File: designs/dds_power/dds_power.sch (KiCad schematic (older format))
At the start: 25 parts, among them K1 3.3_1.8, K2 3.3_1.8, K3 3.3_1.8, K4 3.3_1.8, K5 3.3_1.8, K6 3.3_1.8, P1 CONN_3, P2 12V, P3 12V, P4 12V, P5 12V, P6 12V, P7 12V, U1 QD48T018033

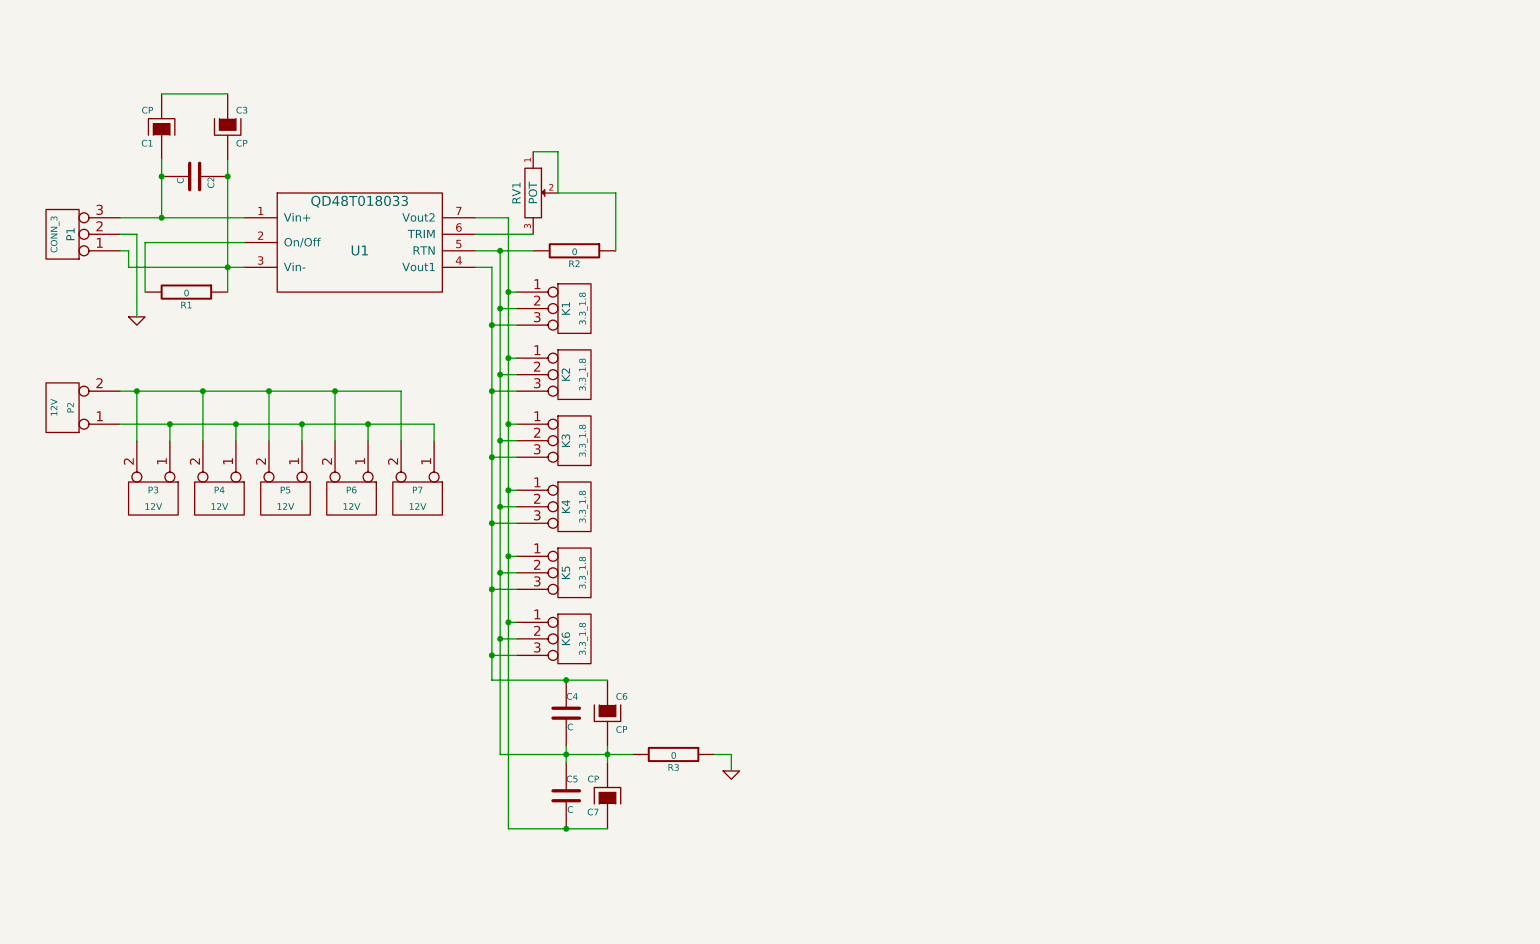
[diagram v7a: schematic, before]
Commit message: [designs/dds_power] update for new power requirements
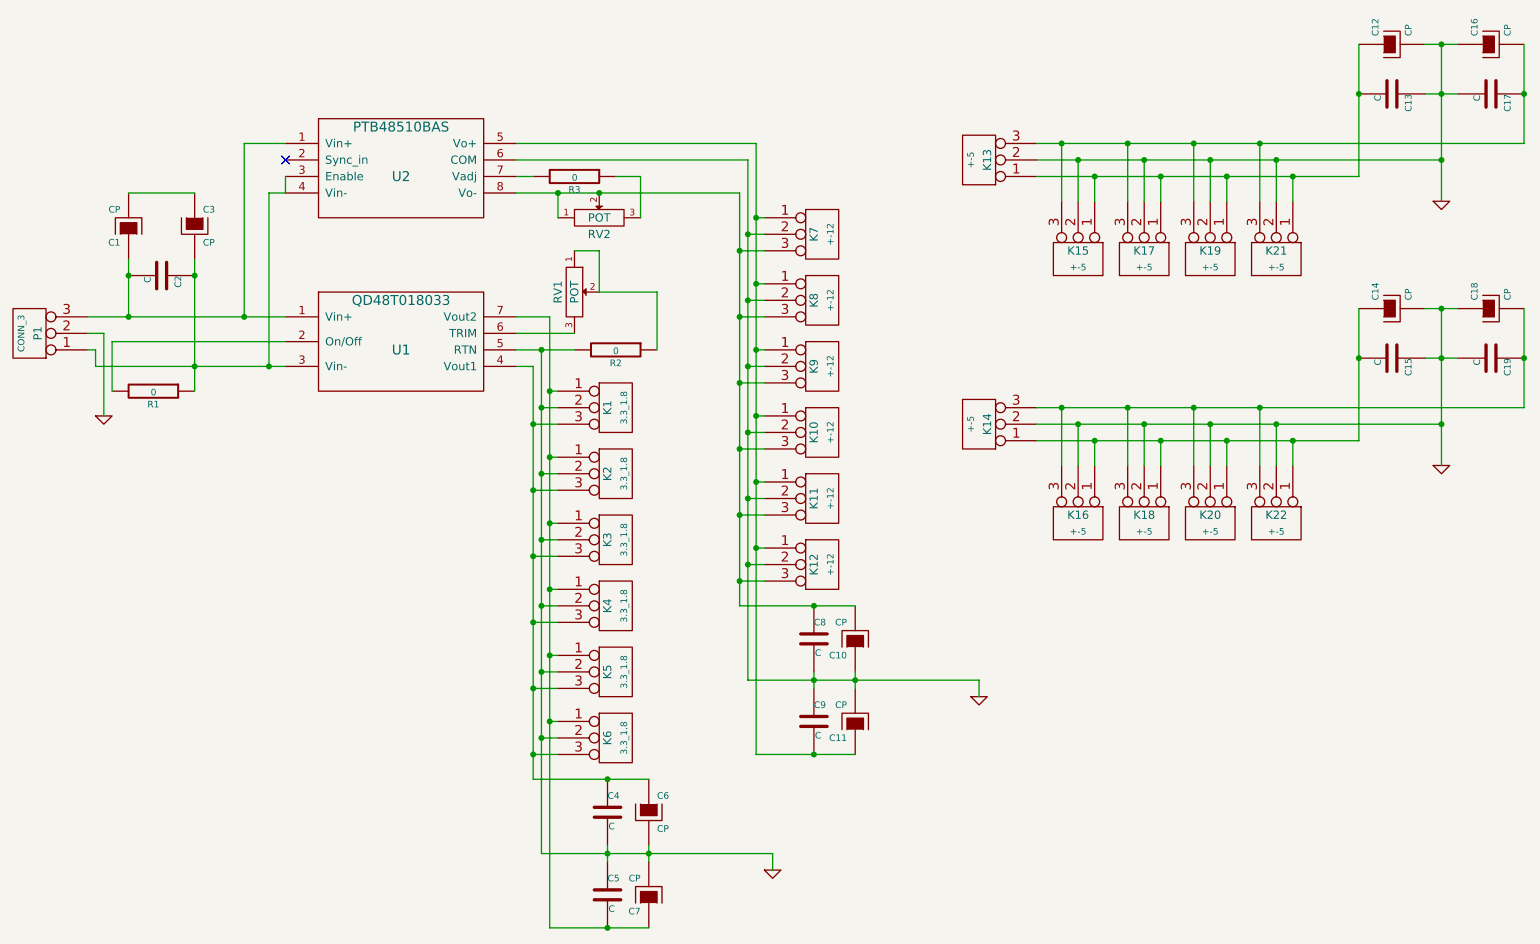
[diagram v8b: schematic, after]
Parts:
- removed P2, P3, P4, P5, P6, P7: 12V, cmr_link:2-pins_150mil, symbol CONN_2
- added C10, C11, C12, C14, C16, C18: CP, Capacitors_ThroughHole:C_Radial_D5_L11_P2, symbol CP-RESCUE-dds_power
- added C13, C15, C17, C19, C8, C9: C, Capacitors_SMD:C_1206, symbol C-RESCUE-dds_power
- added K10, K11, K12, K7, K8, K9: +-12, cmr_link:3-pins_150mil, symbol CONN_3
- added K13, K14, K15, K16, K17, K18, K19, K20, K21, K22: +-5, cmr_link:3-pins_150mil, symbol CONN_3
- added RV2: POT, Potentiometers:Potentiometer_Bourns_3296Y_3-8Zoll_Angular_ScrewUp, symbol POT-RESCUE-dds_power
- added U2: PTB48510BAS, ptb48510bas:ptb48510bas, symbol PTB48510BAS
- RV1: footprint Potentiometers:Potentiometer_Bourns_3005_Angular_ScrewFront -> Potentiometers:Potentiometer_Bourns_3296Y_3-8Zoll_Angular_ScrewUp
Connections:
- net GND: now also C4.2, C5.1, C6.2, C7.2, K1.2 (PM), K2.2 (PM), K3.2 (PM), K4.2 (PM), K5.2 (PM), K6.2 (PM), R2.2, U1.5 (RTN), C10.1, C11.2, C12.2, C13.1, C14.2, C15.1, C16.1, C17.2, C18.1, C19.2, C8.2, C9.1, K10.2 (PM), K11.2 (PM), K12.2 (PM), K13.2 (PM), K14.2 (PM), K15.2 (PM), K16.2 (PM), K17.2 (PM), K18.2 (PM), K19.2 (PM), K20.2 (PM), K21.2 (PM), K22.2 (PM), K7.2 (PM), K8.2 (PM), K9.2 (PM), U2.6 (COM); no longer R3.1
- net at C1.1, C2.2, P1.3 (P3)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: now also U2.1 (Vin+)
- net at C2.1, C3.2, P1.1 (P1)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: now also U2.3 (Enable), U2.4 (Vin-)
- new net: C11.1, C9.2, K10.1 (P1), K11.1 (P1), K12.1 (P1), K7.1 (P1), K8.1 (P1), K9.1 (P1), U2.5 (Vo+)
- new net: R3.2, U2.7 (Vadj)
- new net: C10.2, C8.1, K10.3 (P3), K11.3 (P3), K12.3 (P3), K7.3 (P3), K8.3 (P3), K9.3 (P3), RV2.1, RV2.2, U2.8 (Vo-)
- new net: R3.1, RV2.3
- new net: C14.1, C15.2, K14.1 (P1), K16.1 (P1), K18.1 (P1), K20.1 (P1), K22.1 (P1)
- new net: C18.2, C19.1, K14.3 (P3), K16.3 (P3), K18.3 (P3), K20.3 (P3), K22.3 (P3)
- new net: C12.1, C13.2, K13.1 (P1), K15.1 (P1), K17.1 (P1), K19.1 (P1), K21.1 (P1)
- new net: C16.2, C17.1, K13.3 (P3), K15.3 (P3), K17.3 (P3), K19.3 (P3), K21.3 (P3)
- no-connect marks 0 -> 1
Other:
- moved on the sheet: C1, C2, C3, C4, C5, C6, C7, K1, K2, K3, K4, K5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
